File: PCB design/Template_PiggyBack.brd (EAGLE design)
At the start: 63.5 x 88.6 mm, 46 parts, among them CN1 USB power supply, IC1 MCP6002, IC3 MCP6002, IC4 REG1117

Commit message: worked on pcb layout
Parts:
- moved C5 34.3 mm to (49.5, 71.1), turned to 0 degrees
- moved C2 32.4 mm to (20.3, 61.0), turned to 180 degrees
- moved IC4 30.5 mm to (47.0, 80.0)
- moved R5 30.0 mm to (22.9, 74.9), turned to 180 degrees
- moved TP_GND 29.5 mm to (40.6, 63.5)
- moved C6 25.5 mm to (44.5, 71.1)
- moved R9 23.2 mm to (29.2, 40.6), turned to 180 degrees
- moved IC1 23.0 mm to (22.2, 67.9), turned to 0 degrees
- moved C1 21.7 mm to (15.2, 72.4), turned to 270 degrees
- moved R2 21.7 mm to (30.5, 68.6), turned to 90 degrees
- moved R1 21.6 mm to (15.2, 64.8), turned to 90 degrees
- moved CN1 20.7 mm to (33.0, 7.62), turned to 180 degrees
- moved C10 19.8 mm to (45.7, 63.5)
- moved C9 19.8 mm to (50.8, 63.5)
- moved R3 19.2 mm to (30.5, 62.2)
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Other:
- board text removed: "Sensor-Board Piggy-Back hhrt@zhaw.ch 26.07.2021"

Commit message: PCB Output
changed the PCB Output to PC1 and PC3
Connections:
- removed net PA4: R12.2, TP3.TP
- net PA5: no longer R6.2, TP4.TP
- net PC1_: now also R6.2, TP4.TP
- net PC3: now also R12.2, TP3.TP
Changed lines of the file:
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@@
 </layers>
 <board>
-<fusionsync huburn="a.YnVzaW5lc3M6c3R1ZGVudHM1MjQ1NQ" projecturn="a.YnVzaW5lc3M6c3R1ZGVudHM1MjQ1NSNEMjAyMzAzMTU2MjA4NTg5NzY" f3durn="urn:adsk.wipprod:dm.lineage:P7s-F4vPSu64QmUG7M5eEA" pcbguid="" lastpulledtime="" lastsyncedchangeguid="" latestrevisionid="" lastsyncedrevisionid="" lastboardhashguid="" lastpushedtime="" linktopcb3d="true"/>
+<fusionsync huburn="a.YnVzaW5lc3M6c3R1ZGVudHM1MjQ1NQ" projecturn="a.YnVzaW5lc3M6c3R1ZGVudHM1MjQ1NSNEMjAyMzAzMTU2MjA4NTg5NzY" f3durn="urn:adsk.wipprod:dm.lineage:P7s-F4vPSu64QmUG7M5eEA" pcbguid="" lastpulledtime="" lastsyncedchangeguid="" latestrevisionid="" lastsyncedrevisionid="" lastboardhashguid="" lastpushedtime="" linktopcb3d="false"/>
 <plain>
 <wire x1="0" y1="0" x2="63.48" y2="0" width="0" layer="20"/>
@@
 <signal name="PC1_">
 <contactref element="J2" pad="7"/>
+<contactref element="R6" pad="2"/>
+<contactref element="TP4" pad="TP"/>
+<wire x1="39.37" y1="17.78" x2="49.85" y2="57.15" width="0" layer="19" extent="1-1"/>
+<wire x1="7.62" y1="68.58" x2="49.85" y2="57.15" width="0" layer="19" extent="1-1"/>
 </signal>
 <signal name="PC3">
 <contactref element="J2" pad="8"/>
+<contactref element="R12" pad="2"/>
+<contactref element="TP3" pad="TP"/>
+<wire x1="11.43" y1="43.18" x2="7.62" y2="66.04" width="0" layer="19" extent="1-1"/>
+<wire x1="17.46" y1="43.18" x2="11.43" y2="43.18" width="0" layer="19" extent="1-1"/>
 </signal>
 <signal name="PA5">
 <contactref element="J2" pad="11"/>
-<contactref element="R6" pad="2"/>
-<contactref element="TP4" pad="TP"/>
 <contactref element="R15" pad="1"/>
-<wire x1="39.37" y1="17.78" x2="49.85" y2="57.15" width="0" layer="19" extent="1-1"/>
-<wire x1="35.24" y1="17.78" x2="39.37" y2="17.78" width="0" layer="19" extent="1-1"/>
-<wire x1="7.62" y1="58.42" x2="49.85" y2="57.15" width="0" layer="19" extent="1-1"/>
+<wire x1="35.24" y1="17.78" x2="7.62" y2="58.42" width="0" layer="19" extent="1-1"/>
 </signal>
 <signal name="PE7_">
@@
 <wire x1="28.89" y1="24.13" x2="36.51" y2="29.21" width="0" layer="19" extent="1-1"/>
 </signal>
-<signal name="PA4">
-<contactref element="R12" pad="2"/>
-<contactref element="TP3" pad="TP"/>
-<wire x1="11.43" y1="43.18" x2="17.46" y2="43.18" width="0" layer="19" extent="1-1"/>
-</signal>
 </signals>

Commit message: finished layout but it is subject to revision
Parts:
- moved TP6 29.0 mm to (26.7, 80.0)
- moved R9 2.54 mm to (29.2, 43.2)
- moved C16 1.80 mm to (27.9, 29.2)
- moved R10 1.80 mm to (36.8, 41.9)
- moved C13 1.27 mm to (15.2, 36.8)
- moved C15 1.27 mm to (15.2, 30.5)
- moved R12 1.27 mm to (15.2, 43.2)
- moved C1 1.27 mm to (14.0, 72.4)
- moved C11 1.27 mm to (30.5, 35.6)
- moved C14 1.27 mm to (27.9, 22.9)
- moved C17 1.27 mm to (38.1, 22.9)
- moved R1 1.27 mm to (14.0, 64.8)
- moved R14 1.27 mm to (21.6, 29.2)
- moved C12 1.27 mm to (36.8, 35.6)
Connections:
- net VCO: no longer R15.2
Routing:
- net GND: track 0.00 -> 357.9 mm
- net +3V3: track 0.00 -> 131.5 mm, vias 0 -> 2
- net +5V: track 0.00 -> 103.1 mm, vias 0 -> 2
- net PC1_: track 0.00 -> 98.6 mm
- net VCO: track 0.00 -> 76.4 mm
- net PA5: track 0.00 -> 57.9 mm
- net N$8: track 0.00 -> 54.0 mm
- net IF_Q: track 0.00 -> 51.2 mm, vias 0 -> 1
- net N$7: track 0.00 -> 44.4 mm
- net N$9: track 0.00 -> 37.7 mm
- net N$2: track 0.00 -> 30.6 mm
- net PC3: track 0.00 -> 29.5 mm
- net V_GND: track 0.00 -> 28.6 mm, vias 0 -> 2
- net N$12: track 0.00 -> 26.9 mm, vias 0 -> 3
- net N$13: track 0.00 -> 25.5 mm
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
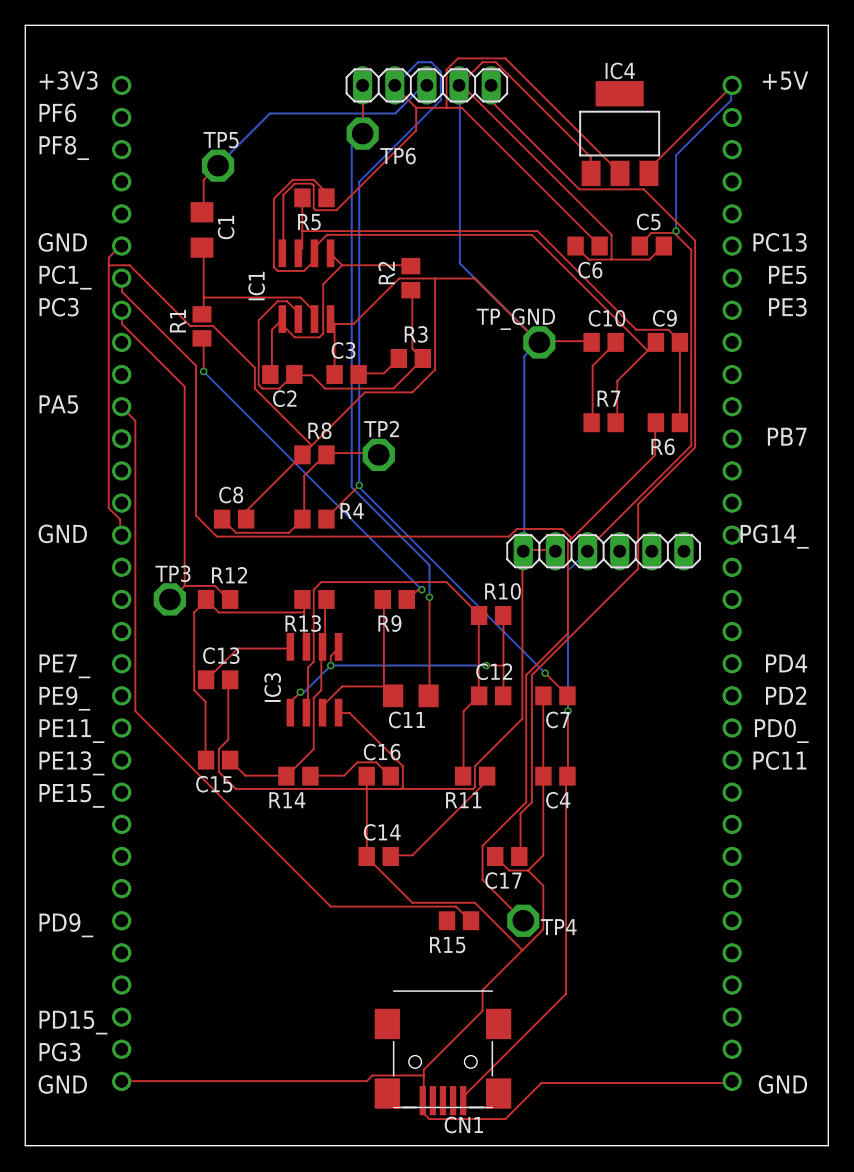
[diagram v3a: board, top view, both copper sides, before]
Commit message: stil some errors in the layout because of width
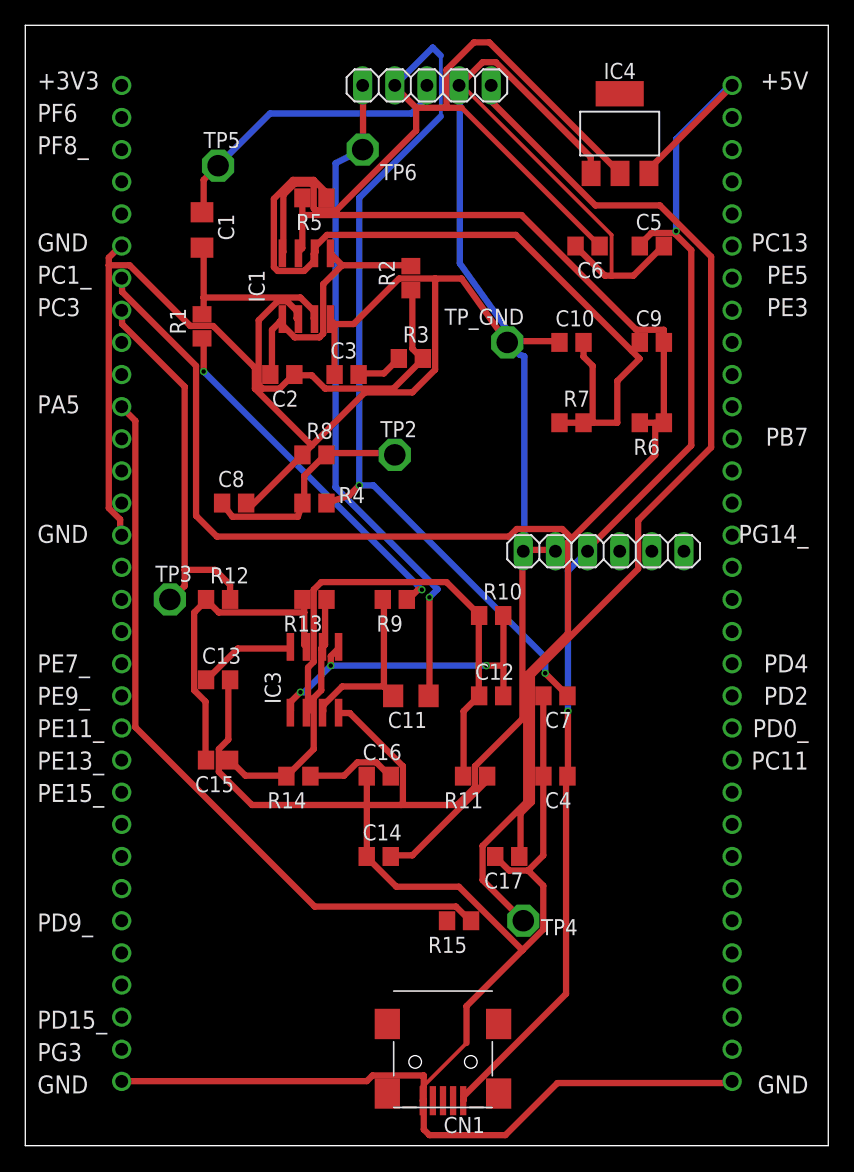
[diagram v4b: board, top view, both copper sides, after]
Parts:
- moved C10 2.54 mm to (43.2, 63.5)
- moved R7 2.54 mm to (43.2, 57.1)
- moved TP_GND 2.54 mm to (38.1, 63.5)
- moved TP6 1.27 mm to (26.7, 78.7)
- moved TP2 1.27 mm to (29.2, 54.6)
- moved C8 1.27 mm to (16.5, 50.8)
- moved C9 1.27 mm to (49.5, 63.5)
- moved R4 1.27 mm to (22.9, 50.8)
- moved R6 1.27 mm to (49.5, 57.1)
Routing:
- net GND: track 357.9 -> 361.2 mm
- net +3V3: track 131.5 -> 134.2 mm
- net N$3: track 7.18 -> 9.27 mm
- net IF_Q: track 51.2 -> 53.2 mm
- net N$8: track 54.0 -> 55.3 mm
- net PC3: track 29.5 -> 30.7 mm
- net PC1_: track 98.6 -> 99.7 mm
- net VCO: track 76.4 -> 77.4 mm
- net PA5: track 57.9 -> 58.6 mm
- net IF_I: track 23.4 -> 24.0 mm

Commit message: layout mission complete
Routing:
- net GND: track 361.2 -> 426.9 mm, vias 0 -> 4
- net +3V3: track 134.2 -> 150.6 mm, vias 2 -> 0
- net N$8: track 55.3 -> 40.8 mm
- net N$9: track 37.7 -> 27.2 mm
- net PC1_: track 99.7 -> 89.5 mm, vias 0 -> 1
- net N$12: track 26.9 -> 32.0 mm, vias 3 -> 0
- net VCO: track 77.4 -> 72.9 mm
- net +5V: track 103.2 -> 107.4 mm, vias 2 -> 0
- net IF_Q: track 53.2 -> 57.3 mm
- net N$3: track 9.27 -> 7.18 mm
- net N$5: track 22.0 -> 23.8 mm
- net N$7: track 44.2 -> 45.9 mm
- net N$2: track 30.6 -> 31.9 mm
- net VCC: track 7.74 -> 8.95 mm
- net V_GND: track 28.6 -> 27.5 mm
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
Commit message: better layout version
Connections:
- net PA5: now also R15.2; no longer R15.1
- net VCO: now also R15.1
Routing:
- net GND: track 426.9 -> 336.4 mm, vias 4 -> 5
- net IF_Q: track 57.3 -> 75.8 mm
- net +5V: track 107.4 -> 121.5 mm, vias 0 -> 1
- net VCO: track 72.9 -> 80.6 mm, vias 0 -> 1
- net PC1_: track 89.5 -> 92.2 mm
- net PA5: track 58.4 -> 56.3 mm
- net +3V3: track 150.6 -> 148.9 mm
- net N$12: track 32.0 -> 32.8 mm

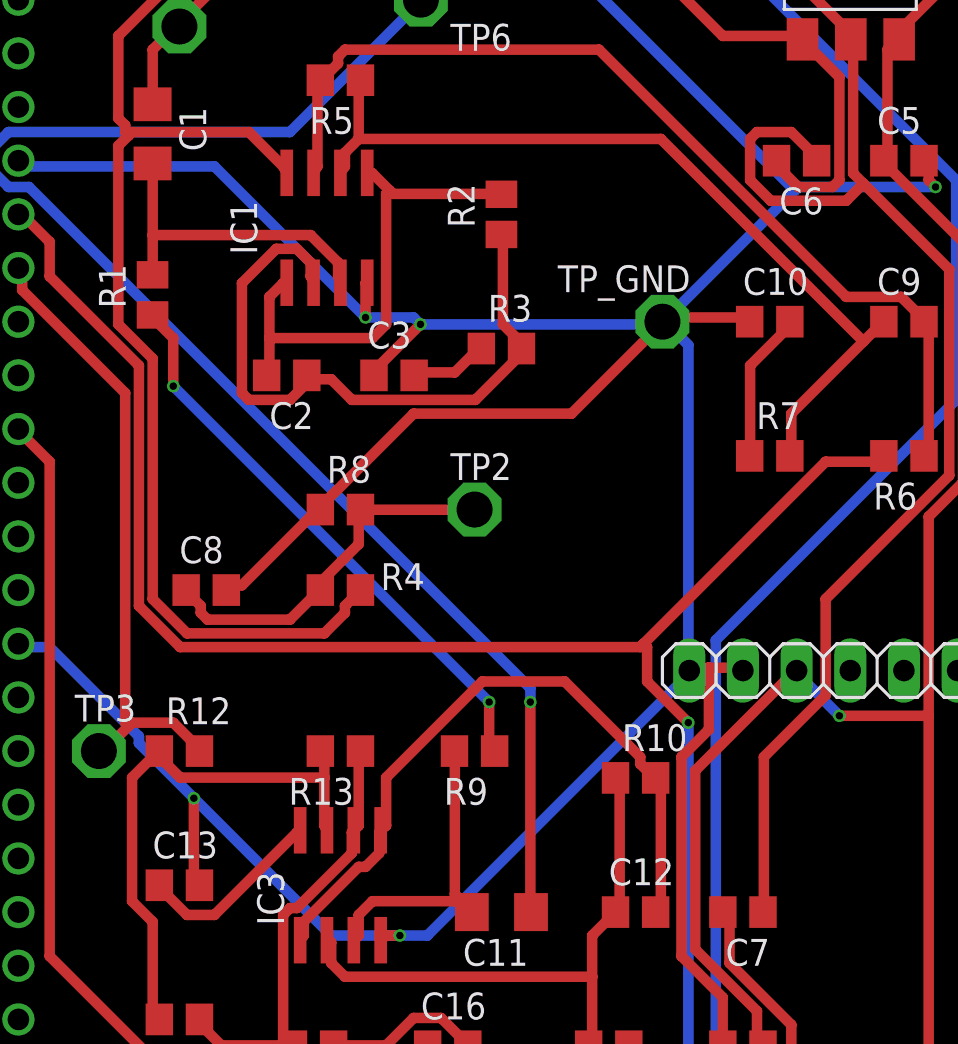
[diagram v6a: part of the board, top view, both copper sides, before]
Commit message: errors in layout fixed
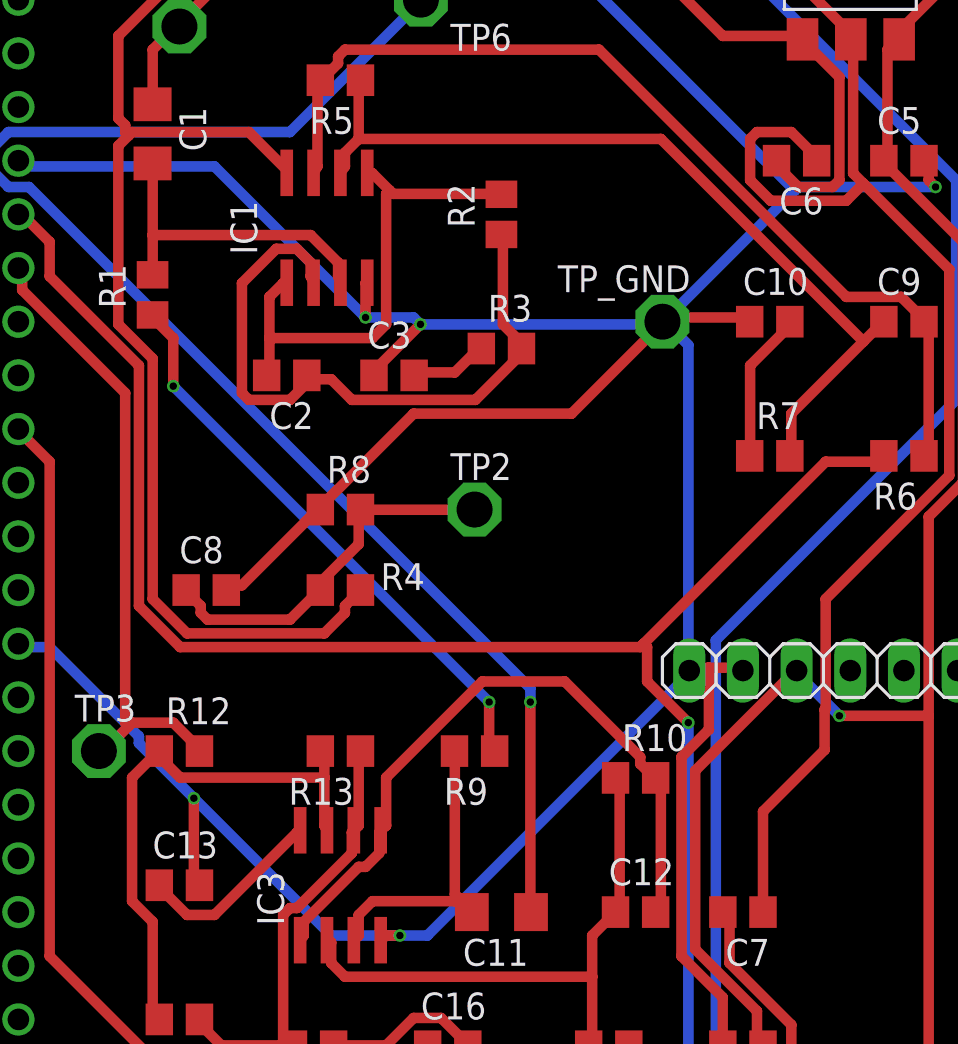
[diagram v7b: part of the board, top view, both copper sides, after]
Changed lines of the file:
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@@
 </layers>
 <board>
-<fusionsync huburn="a.YnVzaW5lc3M6c3R1ZGVudHM1MjQ1NQ" projecturn="a.YnVzaW5lc3M6c3R1ZGVudHM1MjQ1NSNEMjAyMzAzMTU2MjA4NTg5NzY" f3durn="urn:adsk.wipprod:dm.lineage:P7s-F4vPSu64QmUG7M5eEA" pcbguid="" lastpulledtime="" lastsyncedchangeguid="" latestrevisionid="" lastsyncedrevisionid="" lastboardhashguid="" lastpushedtime="" linktopcb3d="false"/>
+<fusionsync huburn="a.YnVzaW5lc3M6c3R1ZGVudHM1MjQ1NQ" projecturn="a.YnVzaW5lc3M6c3R1ZGVudHM1MjQ1NSNEMjAyMzAzMTU2MjA4NTg5NzY" f3durn="urn:adsk.wipprod:dm.lineage:P7s-F4vPSu64QmUG7M5eEA" pcbguid="" lastpulledtime="" lastsyncedchangeguid="" latestrevisionid="" lastsyncedrevisionid="" lastboardhashguid="" lastpushedtime="" linktopcb3d="true"/>
 <plain>
 <wire x1="0" y1="0" x2="63.48" y2="0" width="0" layer="20"/>
@@
 <contactref element="JP5" pad="2"/>
 <contactref element="R4" pad="2"/>
-<contactref element="IC1" pad="8"/>
-<contactref element="C7" pad="1"/>
 <wire x1="23.075" y1="50.05" x2="23.725" y2="50.7" width="0.5" layer="1"/>
 <wire x1="23.075" y1="49.725" x2="23.075" y2="50.05" width="0.5" layer="1"/>
@@
 <wire x1="13" y1="72.475" x2="12.8375" y2="72.3125" width="0.5" layer="1"/>
 <wire x1="12.8375" y1="72.3125" x2="12.35" y2="71.825" width="0.5" layer="1"/>
-<wire x1="18.525" y1="72.475" x2="13" y2="72.475" width="0.5" layer="1"/>
-<wire x1="20.15" y1="70.85" x2="18.525" y2="72.475" width="0.5" layer="1"/>
+<wire x1="13" y1="72.475" x2="18.525" y2="72.475" width="0.5" layer="1"/>
 <wire x1="23.725" y1="50.7" x2="23.81" y2="50.8" width="0.5" layer="1"/>
-<wire x1="20.15" y1="70.85" x2="20.32" y2="70.545" width="0.5" layer="1"/>
-<wire x1="42.9" y1="42.9" x2="42.9" y2="35.75" width="0.5" layer="1"/>
-<wire x1="45.825" y1="45.825" x2="42.9" y2="42.9" width="0.5" layer="1"/>
-<wire x1="45.825" y1="50.375" x2="45.825" y2="45.825" width="0.5" layer="1"/>
 <wire x1="51.675" y1="56.225" x2="45.825" y2="50.375" width="0.5" layer="1"/>
 <wire x1="51.675" y1="65.975" x2="51.675" y2="56.225" width="0.5" layer="1"/>
@@
 <wire x1="47.6125" y1="70.0375" x2="51.675" y2="65.975" width="0.5" layer="1"/>
 <wire x1="47.125" y1="76.7" x2="47.125" y2="70.525" width="0.5" layer="1"/>
-<wire x1="42.9" y1="35.75" x2="42.86" y2="35.56" width="0.5" layer="1"/>
 <wire x1="47.125" y1="76.7" x2="47.0154" y2="76.8604" width="0.5" layer="1"/>
 <wire x1="45.175" y1="71.5" x2="45.175" y2="71.175" width="0.5" layer="1"/>
@@
 <wire x1="12.675" y1="72.475" x2="12.8375" y2="72.3125" width="0.5" layer="1"/>
 <wire x1="28.925" y1="83.525" x2="29.21" y2="83.82" width="0.5" layer="1"/>
+<contactref element="IC1" pad="8"/>
+<contactref element="C7" pad="1"/>
+<wire x1="45.825" y1="45.18995" x2="45.775" y2="45.13995" width="0.5" layer="1"/>
+<wire x1="45.775" y1="45.13995" x2="45.775" y2="43.235" width="0.5" layer="1"/>
+<wire x1="42.86" y1="40.32" x2="42.86" y2="35.56" width="0.5" layer="1"/>
+<wire x1="45.825" y1="50.375" x2="45.825" y2="45.18995" width="0.5" layer="1"/>
+<wire x1="45.775" y1="43.235" x2="42.86" y2="40.32" width="0.5" layer="1"/>
+<wire x1="18.525" y1="72.475" x2="20.32" y2="70.68" width="0.5" layer="1"/>
+<wire x1="20.32" y1="70.68" x2="20.32" y2="70.545" width="0.5" layer="1"/>
 </signal>
 <signal name="N$2">
@@
 <mfgpreviewcolor name="substratecolor" color="0xFF786E46"/>
 </mfgpreviewcolors>
-<errors>
-</errors>
 </board>
 </drawing>
